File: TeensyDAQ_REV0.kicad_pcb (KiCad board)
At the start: 2 copper layers, 101.6 x 82.6 mm, 47 parts, among them U100 TPS56637RPAR, U101 DRV8212PDSGR, U102 DRV8212PDSGR, U103 SN65HVD230DR

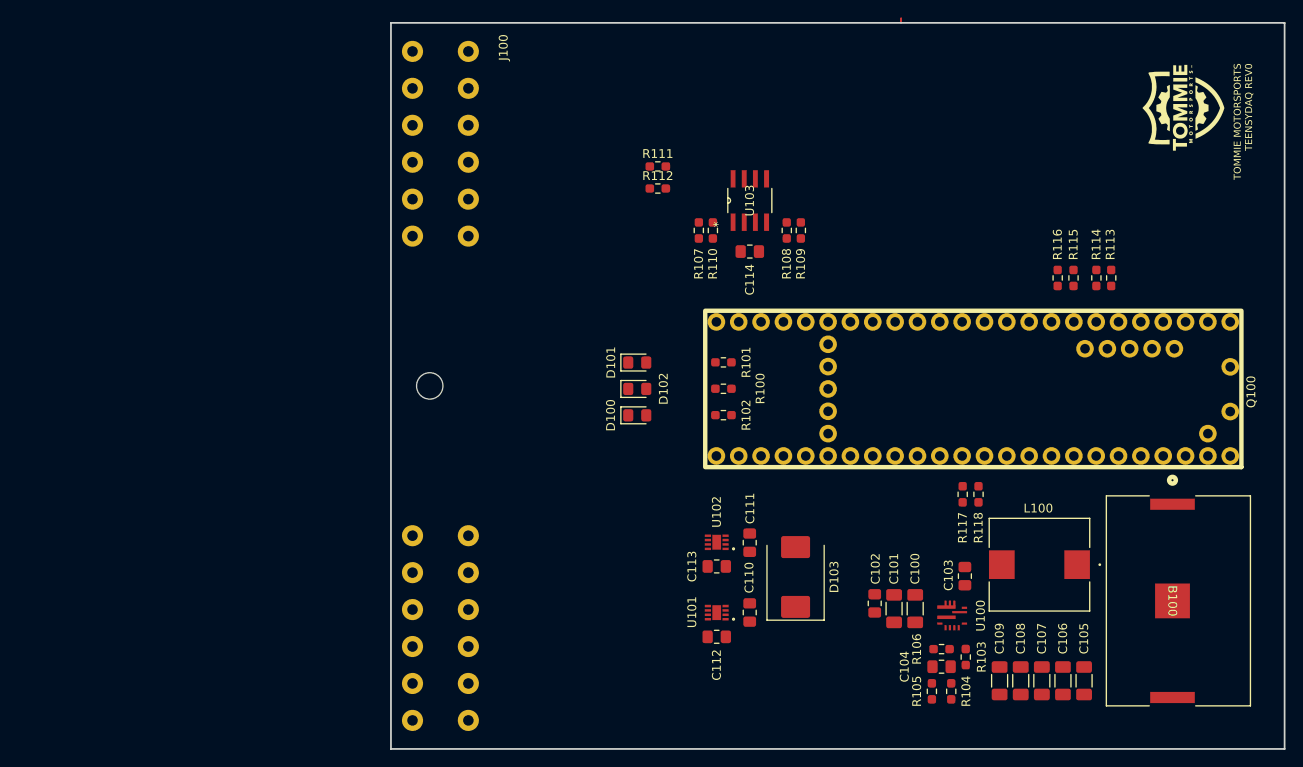
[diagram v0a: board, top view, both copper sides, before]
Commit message: Added gyro, current sense, removed servo control, added temp sense
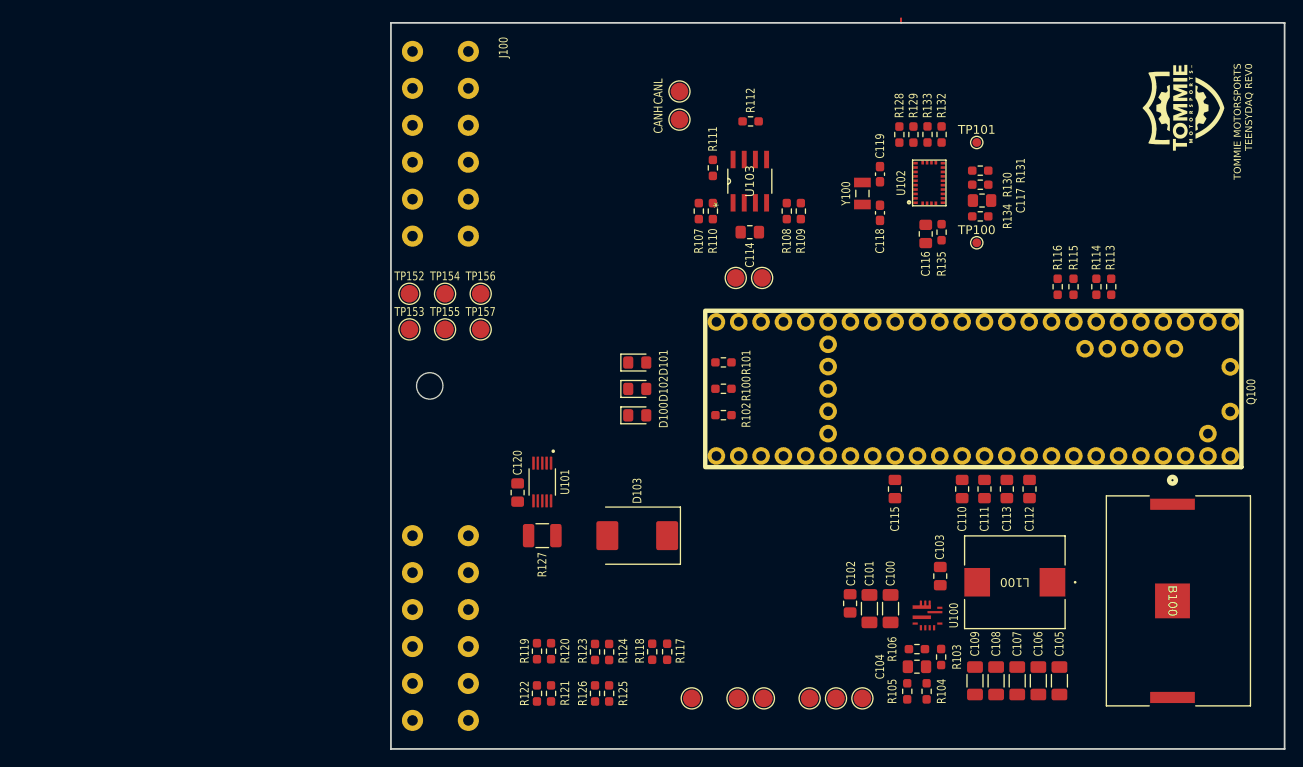
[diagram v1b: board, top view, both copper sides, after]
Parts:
- added C115: 0.1u, Capacitor_SMD:C_0805_2012Metric_Pad1.18x1.45mm_HandSolder, F.Cu at (157.3, 103.0)
- added C116: 100n, Capacitor_SMD:C_0805_2012Metric_Pad1.18x1.45mm_HandSolder, F.Cu at (160.8, 74.0)
- added C117: 100n, Capacitor_SMD:C_0805_2012Metric_Pad1.18x1.45mm_HandSolder, F.Cu at (167.2, 70.2)
- added C118: 22p, Capacitor_SMD:C_0603_1608Metric_Pad1.08x0.95mm_HandSolder, F.Cu at (155.6, 71.6)
- added C119: 22p, Capacitor_SMD:C_0603_1608Metric_Pad1.08x0.95mm_HandSolder, F.Cu at (155.6, 67.2)
- added C120: 0.1u, Capacitor_SMD:C_0805_2012Metric_Pad1.18x1.45mm_HandSolder, F.Cu at (114.4, 103.4)
- added CANH: TestPoint, TestPoint:TestPoint_Pad_D2.0mm, F.Cu at (132.8, 61.0)
- added CANL: TestPoint, TestPoint:TestPoint_Pad_D2.0mm, F.Cu at (132.8, 57.8)
- added R119: 100k, Resistor_SMD:R_0603_1608Metric_Pad0.98x0.95mm_HandSolder, F.Cu at (116.6, 121.4)
- added R120: DNP, Resistor_SMD:R_0603_1608Metric_Pad0.98x0.95mm_HandSolder, F.Cu at (118.2, 121.4)
- added R121: 100k, Resistor_SMD:R_0603_1608Metric_Pad0.98x0.95mm_HandSolder, F.Cu at (116.6, 126.2)
- added R122: DNP, Resistor_SMD:R_0603_1608Metric_Pad0.98x0.95mm_HandSolder, F.Cu at (118.2, 126.2)
- added R123: DNP, Resistor_SMD:R_0603_1608Metric_Pad0.98x0.95mm_HandSolder, F.Cu at (123.2, 121.5)
- added R124: DNP, Resistor_SMD:R_0603_1608Metric_Pad0.98x0.95mm_HandSolder, F.Cu at (124.8, 121.5)
- added R125: DNP, Resistor_SMD:R_0603_1608Metric_Pad0.98x0.95mm_HandSolder, F.Cu at (123.2, 126.2)
- added R126: DNP, Resistor_SMD:R_0603_1608Metric_Pad0.98x0.95mm_HandSolder, F.Cu at (124.8, 126.2)
- added R127: 0.1, Resistor_SMD:R_1210_3225Metric_Pad1.30x2.65mm_HandSolder, F.Cu at (117.2, 108.3)
- added R128: 10k, Resistor_SMD:R_0603_1608Metric_Pad0.98x0.95mm_HandSolder, F.Cu at (157.8, 62.7)
- added R129: 10k, Resistor_SMD:R_0603_1608Metric_Pad0.98x0.95mm_HandSolder, F.Cu at (159.4, 62.7)
- added R130: 0, Resistor_SMD:R_0603_1608Metric_Pad0.98x0.95mm_HandSolder, F.Cu at (167.0, 68.4)
- added R131: 0, Resistor_SMD:R_0603_1608Metric_Pad0.98x0.95mm_HandSolder, F.Cu at (167.0, 66.8)
- added R132: 0, Resistor_SMD:R_0603_1608Metric_Pad0.98x0.95mm_HandSolder, F.Cu at (162.6, 62.7)
- added R133: 10k, Resistor_SMD:R_0603_1608Metric_Pad0.98x0.95mm_HandSolder, F.Cu at (161.0, 62.7)
- added R134: 10k, Resistor_SMD:R_0603_1608Metric_Pad0.98x0.95mm_HandSolder, F.Cu at (167.0, 72.0)
- added R135: 10k, Resistor_SMD:R_0603_1608Metric_Pad0.98x0.95mm_HandSolder, F.Cu at (162.6, 73.8)
- added TP100: TestPoint, TestPoint:TestPoint_Pad_D1.0mm, F.Cu at (166.6, 75.0)
- added TP101: TestPoint, TestPoint:TestPoint_Pad_D1.0mm, F.Cu at (166.6, 63.6)
- added TP110: TestPoint, TestPoint:TestPoint_Pad_D2.0mm, F.Cu at (139.2, 79.0)
- added TP111: TestPoint, TestPoint:TestPoint_Pad_D2.0mm, F.Cu at (142.2, 79.0)
- added TP114: TestPoint, TestPoint:TestPoint_Pad_D2.0mm, F.Cu at (153.6, 126.8)
- added TP115: TestPoint, TestPoint:TestPoint_Pad_D2.0mm, F.Cu at (147.6, 126.8)
- added TP116: TestPoint, TestPoint:TestPoint_Pad_D2.0mm, F.Cu at (150.6, 126.8)
- added TP117: TestPoint, TestPoint:TestPoint_Pad_D2.0mm, F.Cu at (142.4, 126.8)
- added TP118: TestPoint, TestPoint:TestPoint_Pad_D2.0mm, F.Cu at (139.4, 126.8)
- added TP119: TestPoint, TestPoint:TestPoint_Pad_D2.0mm, F.Cu at (134.2, 126.8)
- added TP152: TestPoint, TestPoint:TestPoint_Pad_D2.0mm, F.Cu at (102.1, 80.8)
- added TP153: TestPoint, TestPoint:TestPoint_Pad_D2.0mm, F.Cu at (102.1, 84.8)
- added TP154: TestPoint, TestPoint:TestPoint_Pad_D2.0mm, F.Cu at (106.2, 80.8)
- added TP155: TestPoint, TestPoint:TestPoint_Pad_D2.0mm, F.Cu at (106.2, 84.8)
- added TP156: TestPoint, TestPoint:TestPoint_Pad_D2.0mm, F.Cu at (110.2, 80.8)
- added TP157: TestPoint, TestPoint:TestPoint_Pad_D2.0mm, F.Cu at (110.2, 84.8)
- added Y100: ABS07-32.768KHZ-T, ABS07_32_768KHZ_T:XTAL_ABS07-32.768KHZ-T, F.Cu at (153.6, 69.4)
- R111: value 10k -> 0
- U101: value DRV8212PDSGR -> INA226AIDGSR; footprint DRV8212PDSGR:WSON8_DSG_TEX -> INA226AIDGSR:INA226AIDGSR
- U102: value DRV8212PDSGR -> BNO055; footprint DRV8212PDSGR:WSON8_DSG_TEX -> BNO055:LGA28R50P4X10_380X520X100
- moved U102 47.5 mm to (161.2, 68.2), turned to 90 degrees
- moved R118 41.2 mm to (129.7, 121.5)
- moved C112 39.3 mm to (172.6, 103.0), turned to -90 degrees
- moved R117 38.1 mm to (131.4, 121.5)
- moved C113 34.1 mm to (170.0, 103.0), turned to -90 degrees
- moved C110 27.9 mm to (164.9, 103.0), turned to -90 degrees
- moved C111 27.4 mm to (167.5, 103.0)
- moved U101 24.8 mm to (117.2, 102.2), turned to -90 degrees
- moved D103 18.6 mm to (128.0, 108.3), turned to 180 degrees
- moved R112 13.0 mm to (140.9, 61.2), turned to 180 degrees
- moved R111 6.26 mm to (136.6, 66.5), turned to -90 degrees
- moved L100 3.44 mm to (170.9, 113.6)
- moved C102 2.80 mm to (152.2, 116.0)
- moved C103 2.80 mm to (162.5, 112.9)
- moved C105 2.80 mm to (176.0, 124.8)
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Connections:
- C100 pad 2: /Analog/Battery_IN+ -> /Enclosure Connectors/Power_OUT+
- C101 pad 2: /Analog/Battery_IN+ -> /Enclosure Connectors/Power_OUT+
- C102 pad 2: /Analog/Battery_IN+ -> /Enclosure Connectors/Power_OUT+
- C110 pad 1: GND -> /Analog/Engine_Thermistor+
- C110 pad 2: Motor_Power+ -> GND
- C111 pad 1: GND -> /Analog/CVT_Thermistor+
- C111 pad 2: Motor_Power+ -> GND
- C112 pad 1: GND -> /Analog/VDIV1_u
- C112 pad 2: +3V3 -> GND
- C113 pad 1: GND -> /Analog/VDIV2_u
- C113 pad 2: +3V3 -> GND
- D103 pad 1: Motor_Power+ -> /Enclosure Connectors/Power_OUT+
- D103 pad 2: /Analog/Battery_IN+ -> CUR_S_-
- J100 pad 10: unconnected-(J100-Pin_10_1-Pad10) -> Net-(J100-Pin_10_1)
- J100 pad 13: /Analog/Battery_IN+ -> CUR_S_+
- J100 pad 14: /Enclosure Connectors/Servo_Pin1_1 -> /Enclosure Connectors/Power_OUT+
- J100 pad 15: /Enclosure Connectors/Servo_Pin2_1 -> Net-(J100-Pin_3_2)
- J100 pad 16: /Enclosure Connectors/Servo_Pin6_1 -> GND
- J100 pad 17: /Differential Control/Motor_Out1_1 -> /Analog/Engine_Thermistor+
- J100 pad 18: /Differential Control/Motor_Out1_2 -> /Analog/CVT_Thermistor+
- J100 pad 19: /Differential Control/Motor_Out2_2 -> /Analog/VDIV1+
- J100 pad 20: /Differential Control/Motor_Out2_1 -> /Analog/VDIV2+
- J100 pad 21: /Enclosure Connectors/Servo_Pin6_2 -> Net-(J100-Pin_9_2)
- J100 pad 22: /Enclosure Connectors/Servo_Pin2_2 -> Net-(J100-Pin_10_2)
- J100 pad 23: /Enclosure Connectors/Servo_Pin1_2 -> /Enclosure Connectors/Power_OUT+
- J100 pad 4: unconnected-(J100-Pin_4_1-Pad4) -> Net-(J100-Pin_4_1)
- J100 pad 5: unconnected-(J100-Pin_5_1-Pad5) -> /Enclosure Connectors/USB_D-
- J100 pad 8: unconnected-(J100-Pin_8_1-Pad8) -> /Enclosure Connectors/USB_D+
- J100 pad 9: unconnected-(J100-Pin_9_1-Pad9) -> Net-(J100-Pin_9_1)
- Q100 pad -1: unconnected-(Q100-GND-Pad-1) -> GND
- Q100 pad -13: unconnected-(Q100-GND-Pad-13) -> GND
- Q100 pad -14: unconnected-(Q100-GND-Pad-14) -> GND
- Q100 pad -17: unconnected-(Q100-GND-Pad-17) -> GND
- Q100 pad -18: unconnected-(Q100-3.3V-Pad-18) -> +3V3
- Q100 pad -4: unconnected-(Q100-GND-Pad-4) -> GND
- Q100 pad -6: unconnected-(Q100-GND-Pad-6) -> GND
- Q100 pad -8: unconnected-(Q100-D-_Device-Pad-8) -> /Enclosure Connectors/USB_D-
- Q100 pad -9: unconnected-(Q100-D+_Device-Pad-9) -> /Enclosure Connectors/USB_D+
- Q100 pad 14: /Analog/VMeas_BATu -> /Analog/Engine_Thermistor+
- Q100 pad 15: unconnected-(Q100-Pad15) -> /Analog/CVT_Thermistor+
- Q100 pad 16: unconnected-(Q100-Pad16) -> /Analog/VDIV2_u
- Q100 pad 17: unconnected-(Q100-Pad17) -> /Analog/VDIV1_u
- Q100 pad 18: unconnected-(Q100-Pad18) -> /Gyro/I2C_SDA
- Q100 pad 19: unconnected-(Q100-Pad19) -> /Gyro/I2C_SCL
- Q100 pad 23: unconnected-(Q100-Pad23) -> /Power Biasing/INA226A_ALERT
- Q100 pad 26: /Enclosure Connectors/Servo_Pin6_1 -> unconnected-(Q100-Pad26)
- Q100 pad 27: /Enclosure Connectors/Servo_Pin1_2 -> unconnected-(Q100-Pad27)
- Q100 pad 28: /Enclosure Connectors/Servo_Pin2_2 -> unconnected-(Q100-Pad28)
- Q100 pad 29: /Enclosure Connectors/Servo_Pin6_2 -> unconnected-(Q100-Pad29)
- Q100 pad 36: /Differential Control/Motor_Driver_IN2_1 -> unconnected-(Q100-Pad36)
- Q100 pad 37: /Differential Control/Motor_Driver_IN1_1 -> unconnected-(Q100-Pad37)
- Q100 pad 40: /Differential Control/Motor_Driver_Sleep2 -> unconnected-(Q100-Pad40)
- Q100 pad 41: /Differential Control/Motor_Driver_Sleep1 -> /Analog/VMeas_BATu
- R117 pad 2: /Analog/Battery_IN+ -> CUR_S_+
- U100 pad 8: /Analog/Battery_IN+ -> /Enclosure Connectors/Power_OUT+
- U101 pad 1: Motor_Power+ -> GND
- U101 pad 2: /Differential Control/Motor_Out1_1 -> GND
- U101 pad 3: /Differential Control/Motor_Out2_1 -> /Power Biasing/INA226A_ALERT
- U101 pad 4: GND -> /Gyro/I2C_SDA
- U101 pad 5: /Differential Control/Motor_Driver_IN2_1 -> /Gyro/I2C_SCL
- U101 pad 6: /Differential Control/Motor_Driver_IN1_1 -> +3V3
- U101 pad 7: /Differential Control/Motor_Driver_Sleep1 -> GND
- U101 pad 8: +3V3 -> CUR_S_+
- U101 pad 9: GND -> CUR_S_-
- U102 pad 1: Motor_Power+ -> (no net)
- U102 pad 2: /Differential Control/Motor_Out1_2 -> GND
- U102 pad 3: /Differential Control/Motor_Out2_2 -> +3V3
- U102 pad 4: GND -> +3V3
- U102 pad 5: /Differential Control/Motor_Driver_IN2_1 -> Net-(U102-PS1)
- U102 pad 6: /Differential Control/Motor_Driver_IN1_1 -> Net-(U102-PS0)
- U102 pad 7: /Differential Control/Motor_Driver_Sleep2 -> (no net)
- U102 pad 8: +3V3 -> (no net)
- U102 pad 9: GND -> Net-(U102-CAP)
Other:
- board text added: "CHARLIE MILLHOLLIN 2-10-2025"

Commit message: finished up schematic, added magnetic sensor, cleaned up pins, etc.
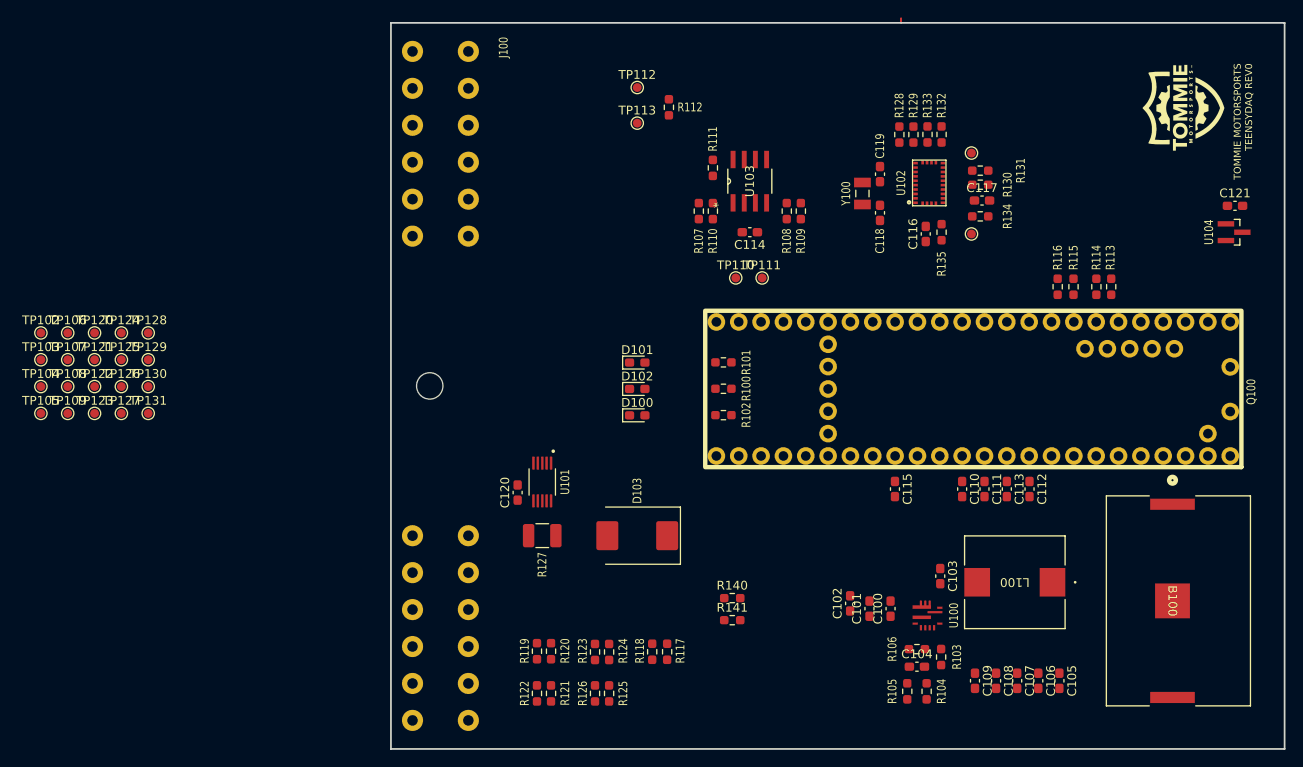
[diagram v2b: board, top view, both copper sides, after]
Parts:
- removed CANH, CANL, TP114, TP115, TP116, TP117, TP118, TP119, TP152, TP153, TP154, TP155, TP156, TP157: TestPoint, TestPoint:TestPoint_Pad_D2.0mm
- added C121: 0.1u, Capacitor_SMD:C_0603_1608Metric_Pad1.08x0.95mm_HandSolder, F.Cu at (196.0, 70.8)
- added R140: 0, Resistor_SMD:R_0603_1608Metric_Pad0.98x0.95mm_HandSolder, F.Cu at (138.8, 115.4)
- added R141: 0, Resistor_SMD:R_0603_1608Metric_Pad0.98x0.95mm_HandSolder, F.Cu at (138.8, 117.9)
- added TP102: TestPoint, TestPoint:TestPoint_Pad_D1.0mm, F.Cu at (60.2, 85.2)
- added TP103: TestPoint, TestPoint:TestPoint_Pad_D1.0mm, F.Cu at (60.2, 88.3)
- added TP104: TestPoint, TestPoint:TestPoint_Pad_D1.0mm, F.Cu at (60.2, 91.3)
- added TP105: TestPoint, TestPoint:TestPoint_Pad_D1.0mm, F.Cu at (60.2, 94.4)
- added TP106: TestPoint, TestPoint:TestPoint_Pad_D1.0mm, F.Cu at (63.2, 85.2)
- added TP107: TestPoint, TestPoint:TestPoint_Pad_D1.0mm, F.Cu at (63.2, 88.3)
- added TP108: TestPoint, TestPoint:TestPoint_Pad_D1.0mm, F.Cu at (63.2, 91.3)
- added TP109: TestPoint, TestPoint:TestPoint_Pad_D1.0mm, F.Cu at (63.2, 94.4)
- added TP112: TestPoint, TestPoint:TestPoint_Pad_D1.0mm, F.Cu at (128.0, 57.4)
- added TP113: TestPoint, TestPoint:TestPoint_Pad_D1.0mm, F.Cu at (128.0, 61.4)
- added TP120: TestPoint, TestPoint:TestPoint_Pad_D1.0mm, F.Cu at (66.3, 85.2)
- added TP121: TestPoint, TestPoint:TestPoint_Pad_D1.0mm, F.Cu at (66.3, 88.3)
- added TP122: TestPoint, TestPoint:TestPoint_Pad_D1.0mm, F.Cu at (66.3, 91.3)
- added TP123: TestPoint, TestPoint:TestPoint_Pad_D1.0mm, F.Cu at (66.3, 94.4)
- added TP124: TestPoint, TestPoint:TestPoint_Pad_D1.0mm, F.Cu at (69.3, 85.2)
- added TP125: TestPoint, TestPoint:TestPoint_Pad_D1.0mm, F.Cu at (69.3, 88.3)
- added TP126: TestPoint, TestPoint:TestPoint_Pad_D1.0mm, F.Cu at (69.3, 91.3)
- added TP127: TestPoint, TestPoint:TestPoint_Pad_D1.0mm, F.Cu at (69.3, 94.4)
- added TP128: TestPoint, TestPoint:TestPoint_Pad_D1.0mm, F.Cu at (72.4, 85.2)
- added TP129: TestPoint, TestPoint:TestPoint_Pad_D1.0mm, F.Cu at (72.4, 88.3)
- added TP130: TestPoint, TestPoint:TestPoint_Pad_D1.0mm, F.Cu at (72.4, 91.3)
- added TP131: TestPoint, TestPoint:TestPoint_Pad_D1.0mm, F.Cu at (72.4, 94.4)
- added U104: DRV5032FBDBZR, DRV5032:DBZ0003A-IPC_A, F.Cu at (195.9, 73.8)
- C100, C101, C105, C106, C107, C108, C109: footprint Capacitor_SMD:C_1206_3216Metric_Pad1.33x1.80mm_HandSolder -> Capacitor_SMD:C_0603_1608Metric_Pad1.08x0.95mm_HandSolder
- C102, C103, C104, C110, C111, C112, C113, C114, C115, C116, C117, C120: footprint Capacitor_SMD:C_0805_2012Metric_Pad1.18x1.45mm_HandSolder -> Capacitor_SMD:C_0603_1608Metric_Pad1.08x0.95mm_HandSolder
- D100, D101, D102: footprint LED_SMD:LED_0805_2012Metric_Pad1.15x1.40mm_HandSolder -> LED_SMD:LED_0603_1608Metric_Pad1.05x0.95mm_HandSolder
- TP110, TP111: footprint TestPoint:TestPoint_Pad_D2.0mm -> TestPoint:TestPoint_Pad_D1.0mm
- moved R112 9.42 mm to (131.6, 59.6), turned to 90 degrees
- moved TP101 1.34 mm to (166.0, 64.8)
- moved TP100 1.17 mm to (166.0, 74.0)
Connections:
- J100 pad 10: Net-(J100-Pin_10_1) -> +5V
- J100 pad 15: Net-(J100-Pin_3_2) -> GND
- J100 pad 16: GND -> /Analog/Engine_Thermistor+
- J100 pad 17: /Analog/Engine_Thermistor+ -> /Analog/VDIV1+
- J100 pad 18: /Analog/CVT_Thermistor+ -> /Enclosure Connectors/P1
- J100 pad 19: /Analog/VDIV1+ -> /Enclosure Connectors/P2
- J100 pad 2: /Analog/Hall_Signal1 -> GND
- J100 pad 21: Net-(J100-Pin_9_2) -> /Analog/CVT_Thermistor+
- J100 pad 22: Net-(J100-Pin_10_2) -> GND
- J100 pad 3: /Analog/Hall_Signal2 -> GND
- J100 pad 4: Net-(J100-Pin_4_1) -> /Analog/Hall_Signal1
- J100 pad 5: /Enclosure Connectors/USB_D- -> /Enclosure Connectors/USB_D+
- J100 pad 6: /CAN/CANL -> /CAN/CANH
- J100 pad 7: /CAN/CANH -> /CAN/CANL
- J100 pad 8: /Enclosure Connectors/USB_D+ -> /Enclosure Connectors/USB_D-
- J100 pad 9: Net-(J100-Pin_9_1) -> /Analog/Hall_Signal2
- Q100 pad 28: unconnected-(Q100-Pad28) -> Net-(Q100-Pad28)
- Q100 pad 29: unconnected-(Q100-Pad29) -> Net-(Q100-Pad29)
- Q100 pad 32: unconnected-(Q100-Pad32) -> /Analog/Magnet_u

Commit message: cleaned up refdes
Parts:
- removed TP112, TP113: TestPoint, TestPoint:TestPoint_Pad_D1.0mm
- moved R140 14.2 mm to (129.6, 126.2), turned to 90 degrees
- moved R141 11.2 mm to (131.2, 126.2), turned to 90 degrees
- moved R112 9.46 mm to (140.8, 61.8), turned to 180 degrees
- moved C102 1.84 mm to (153.4, 117.4)
- moved C120 1.22 mm to (114.6, 102.2)
- moved C101 1.00 mm to (155.0, 117.4)
- moved C100 0.82 mm to (156.6, 117.4)
- moved R134 0.41 mm to (167.1, 71.6)
- moved R135 0.28 mm to (162.4, 74.0)
- moved C117 0.23 mm to (167.1, 70.0)
- moved R117 0.20 mm to (131.2, 121.5)
- moved R118 0.10 mm to (129.6, 121.5)
- moved R130 0.09 mm to (167.1, 68.4)
- moved R131 0.09 mm to (167.1, 66.8)
- renumbered TP111 to RX, TP110 to TX
